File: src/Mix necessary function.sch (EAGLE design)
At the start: 15 parts, among them CON1 XT90PW-M, SW1 02-JST, SW2 02-JST

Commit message: servo2
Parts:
- added LED_SW: SS-12SDP2, SS-12SDP2:SS-12SDP2
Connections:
- new net BLUE: LED.1, LED_SW.L
- new net RED: LED.2, LED_SW.R
- net GND: now also LED_SW.C; no longer LED.1, LED.3
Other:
- note added: "servo(DS3235sg)： voltage 4.8-6.4V current about0.3A regulater 22.2Vから6Vに変圧 allowable loss(許容損失) 16W (22.2-6)*0.3=4.86W no problem"
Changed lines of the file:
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@@
 <part name="C3" library="GRM0335C1E240GA01D" deviceset="GRM0335C1E240GA01D" device="" value="0.1μF"/>
 <part name="C6" library="GRM0335C1E240GA01D" deviceset="GRM0335C1E240GA01D" device="" value="0.1μF"/>
+<part name="LED_SW" library="SS-12SDP2" deviceset="SS-12SDP2" device=""/>
 </parts>
 <sheets>
@@
 <text x="116.84" y="127" size="5.08" layer="97">LEDsupply</text>
 <wire x1="172.72" y1="223.52" x2="172.72" y2="154.94" width="0.1524" layer="97"/>
-<wire x1="172.72" y1="154.94" x2="241.3" y2="154.94" width="0.1524" layer="97"/>
-<wire x1="241.3" y1="154.94" x2="241.3" y2="223.52" width="0.1524" layer="97"/>
-<wire x1="241.3" y1="223.52" x2="172.72" y2="223.52" width="0.1524" layer="97"/>
+<wire x1="172.72" y1="154.94" x2="276.86" y2="154.94" width="0.1524" layer="97"/>
+<wire x1="276.86" y1="154.94" x2="276.86" y2="223.52" width="0.1524" layer="97"/>
+<wire x1="276.86" y1="223.52" x2="172.72" y2="223.52" width="0.1524" layer="97"/>
 <text x="175.26" y="218.44" size="5.08" layer="97">series_regulater</text>
-<text x="180.34" y="157.48" size="1.9304" layer="94">PVCC:22.2V</text>
+<text x="254" y="167.64" size="1.9304" layer="94">PVCC:22.2V</text>
 <wire x1="213.36" y1="88.9" x2="213.36" y2="137.16" width="0.1524" layer="97"/>
 <wire x1="213.36" y1="137.16" x2="266.7" y2="137.16" width="0.1524" layer="97"/>
@@
 ・テープLED用の四心コネクタ
 ・非常停止スイッチ用のAnｄ回路</text>
+<text x="241.3" y="190.5" size="1.778" layer="94">servo(DS3235sg)：
+  voltage 4.8-6.4V
+　current about0.3A
+regulater
+ 22.2Vから6Vに変圧
+ allowable loss(許容損失) 16W
+(22.2-6)*0.3=4.86W
+no problem</text>
 </plain>
 <instances>
@@
 <instance part="P+3" gate="VCC" x="177.8" y="121.92" smashed="yes"/>
 <instance part="P+4" gate="VCC" x="200.66" y="121.92" smashed="yes"/>
-<instance part="SUPPLY4" gate="GND" x="142.24" y="99.06" smashed="yes"/>
+<instance part="SUPPLY4" gate="GND" x="152.4" y="99.06" smashed="yes"/>
 <instance part="U$17" gate="G$1" x="208.28" y="180.34" smashed="yes"/>
 <instance part="C4" gate="G$1" x="193.04" y="175.26" smashed="yes">
@@
 <attribute name="NAME" x="230.124" y="175.641" size="1.778" layer="95"/>
 <attribute name="VALUE" x="230.124" y="170.561" size="1.778" layer="96"/>
+</instance>
+<instance part="LED_SW" gate="G$1" x="147.32" y="104.14" smashed="yes" rot="R90">
+<attribute name="NAME" x="152.4" y="101.6" size="1.778" layer="95" rot="R180"/>
 </instance>
 </instances>
@@
 </segment>
 <segment>
-<pinref part="LED" gate="G$1" pin="3"/>
-<wire x1="134.62" y1="109.22" x2="142.24" y2="109.22" width="0.1524" layer="91"/>
-<pinref part="SUPPLY4" gate="GND" pin="GND"/>
-<pinref part="LED" gate="G$1" pin="1"/>
-<wire x1="142.24" y1="109.22" x2="142.24" y2="104.14" width="0.1524" layer="91"/>
-<wire x1="142.24" y1="104.14" x2="142.24" y2="101.6" width="0.1524" layer="91"/>
-<wire x1="134.62" y1="104.14" x2="142.24" y2="104.14" width="0.1524" layer="91"/>
-<junction x="142.24" y="104.14"/>
-<label x="139.7" y="96.52" size="1.778" layer="95"/>
-</segment>
-<segment>
 <pinref part="AZUSA_CON" gate="G$1" pin="1"/>
 <wire x1="236.22" y1="119.38" x2="241.3" y2="119.38" width="0.1524" layer="91"/>
@@
 <label x="205.74" y="187.96" size="1.778" layer="95"/>
 </segment>
+<segment>
+<pinref part="LED_SW" gate="G$1" pin="C"/>
+<pinref part="SUPPLY4" gate="GND" pin="GND"/>
+<wire x1="152.4" y1="104.14" x2="152.4" y2="101.6" width="0.1524" layer="91"/>
+<label x="149.86" y="96.52" size="1.778" layer="95"/>
+</segment>
 </net>
 <net name="VCC" class="0">
@@
 </segment>
 </net>
+<net name="RED" class="0">
+<segment>
+<pinref part="LED" gate="G$1" pin="2"/>
+<wire x1="134.62" y1="106.68" x2="142.24" y2="106.68" width="0.1524" layer="91"/>
+<pinref part="LED_SW" gate="G$1" pin="R"/>
+<label x="137.16" y="106.68" size="1.778" layer="95"/>
+</segment>
+</net>
+<net name="BLUE" class="0">
+<segment>
+<pinref part="LED" gate="G$1" pin="1"/>
+<wire x1="134.62" y1="104.14" x2="134.62" y2="101.6" width="0.1524" layer="91"/>
+<pinref part="LED_SW" gate="G$1" pin="L"/>
+<wire x1="134.62" y1="101.6" x2="142.24" y2="101.6" width="0.1524" layer="91"/>
+<label x="137.16" y="101.6" size="1.778" layer="95"/>
+</segment>
+</net>

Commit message: necefunc fix
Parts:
- added AZUSA_CON2: 02-JST, con-jst-xh (1):02-JST
- added H1, H2, H3, H4: MOUNT-HOLE3.2, holes:MOUNT-HOLE3.2
- added SERVO2: (no value), con-jst-xh (1):03-JST
- renumbered AZUSA_CON to AZUSA_CON1, SERVO to SERVO1
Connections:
- net PWM_SERVO renamed PWM1_SERVO
- new net PWM2_SERVO: AZUSA_CON2.2, SERVO2.3
- net +6V: now also SERVO2.2
- net GND: now also AZUSA_CON2.1, SERVO2.1
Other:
- note added: "drill"

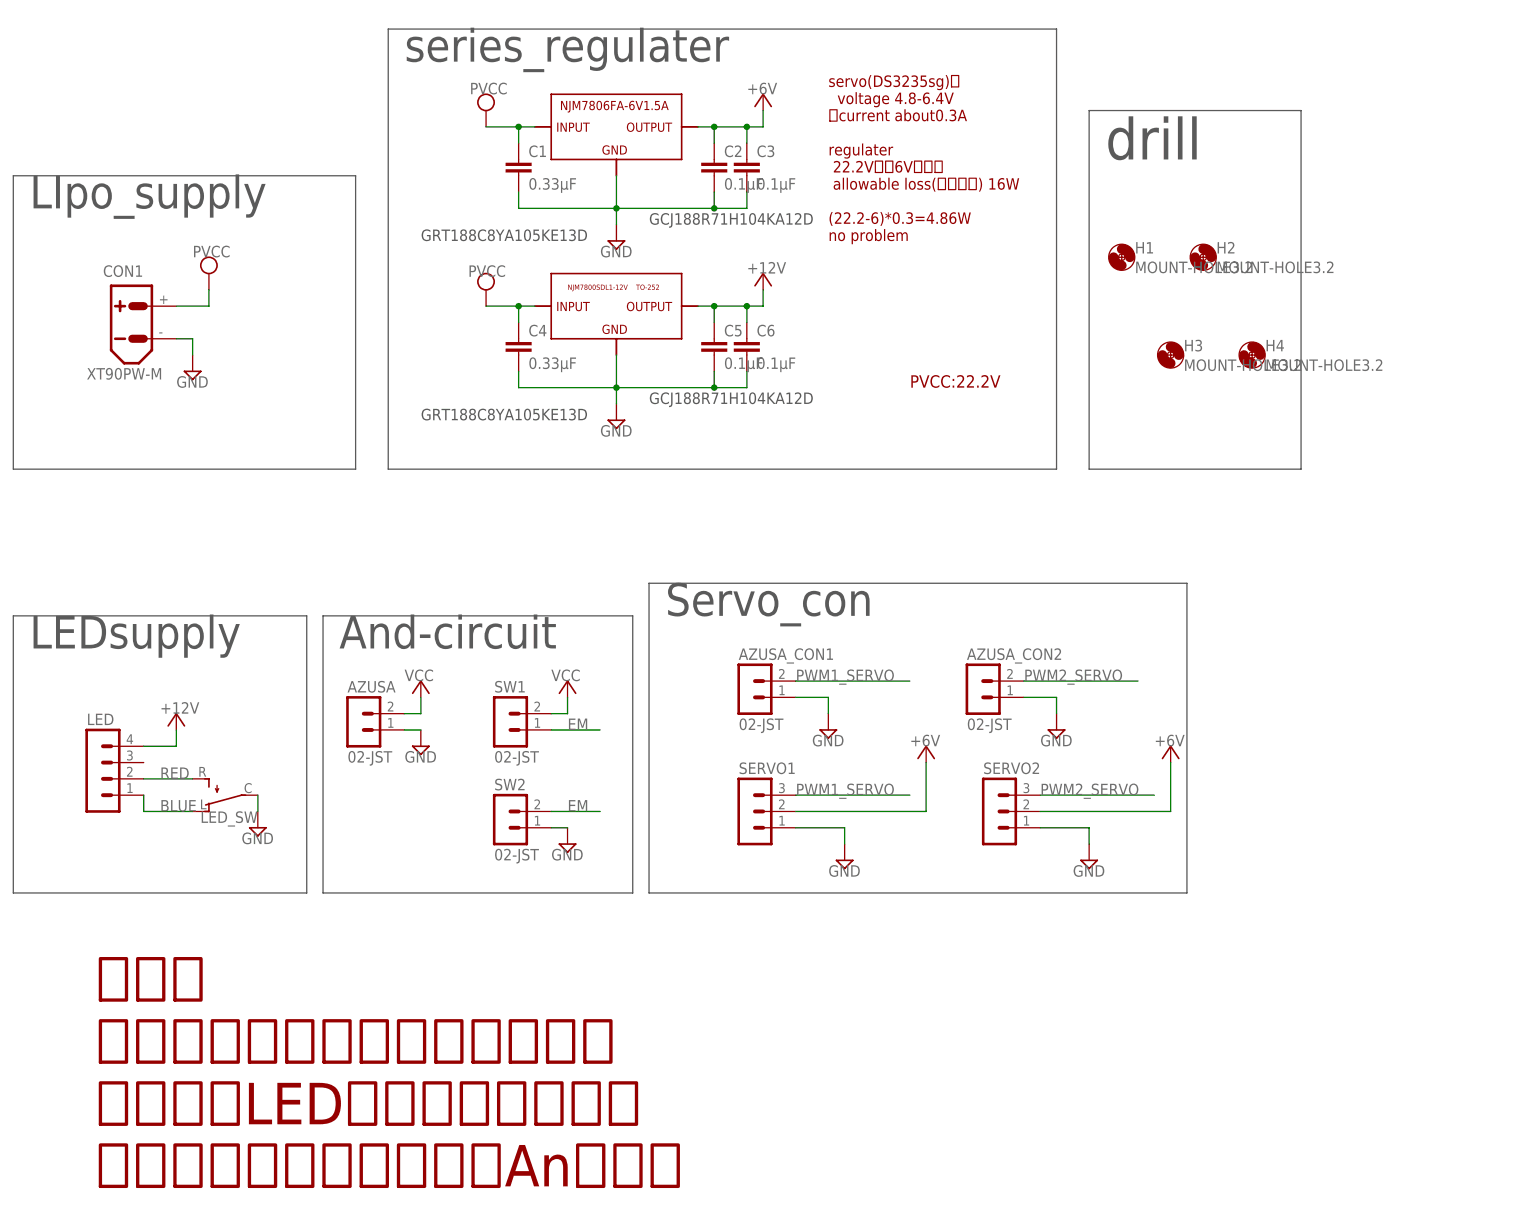
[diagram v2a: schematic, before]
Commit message: fix twelite circuit slot
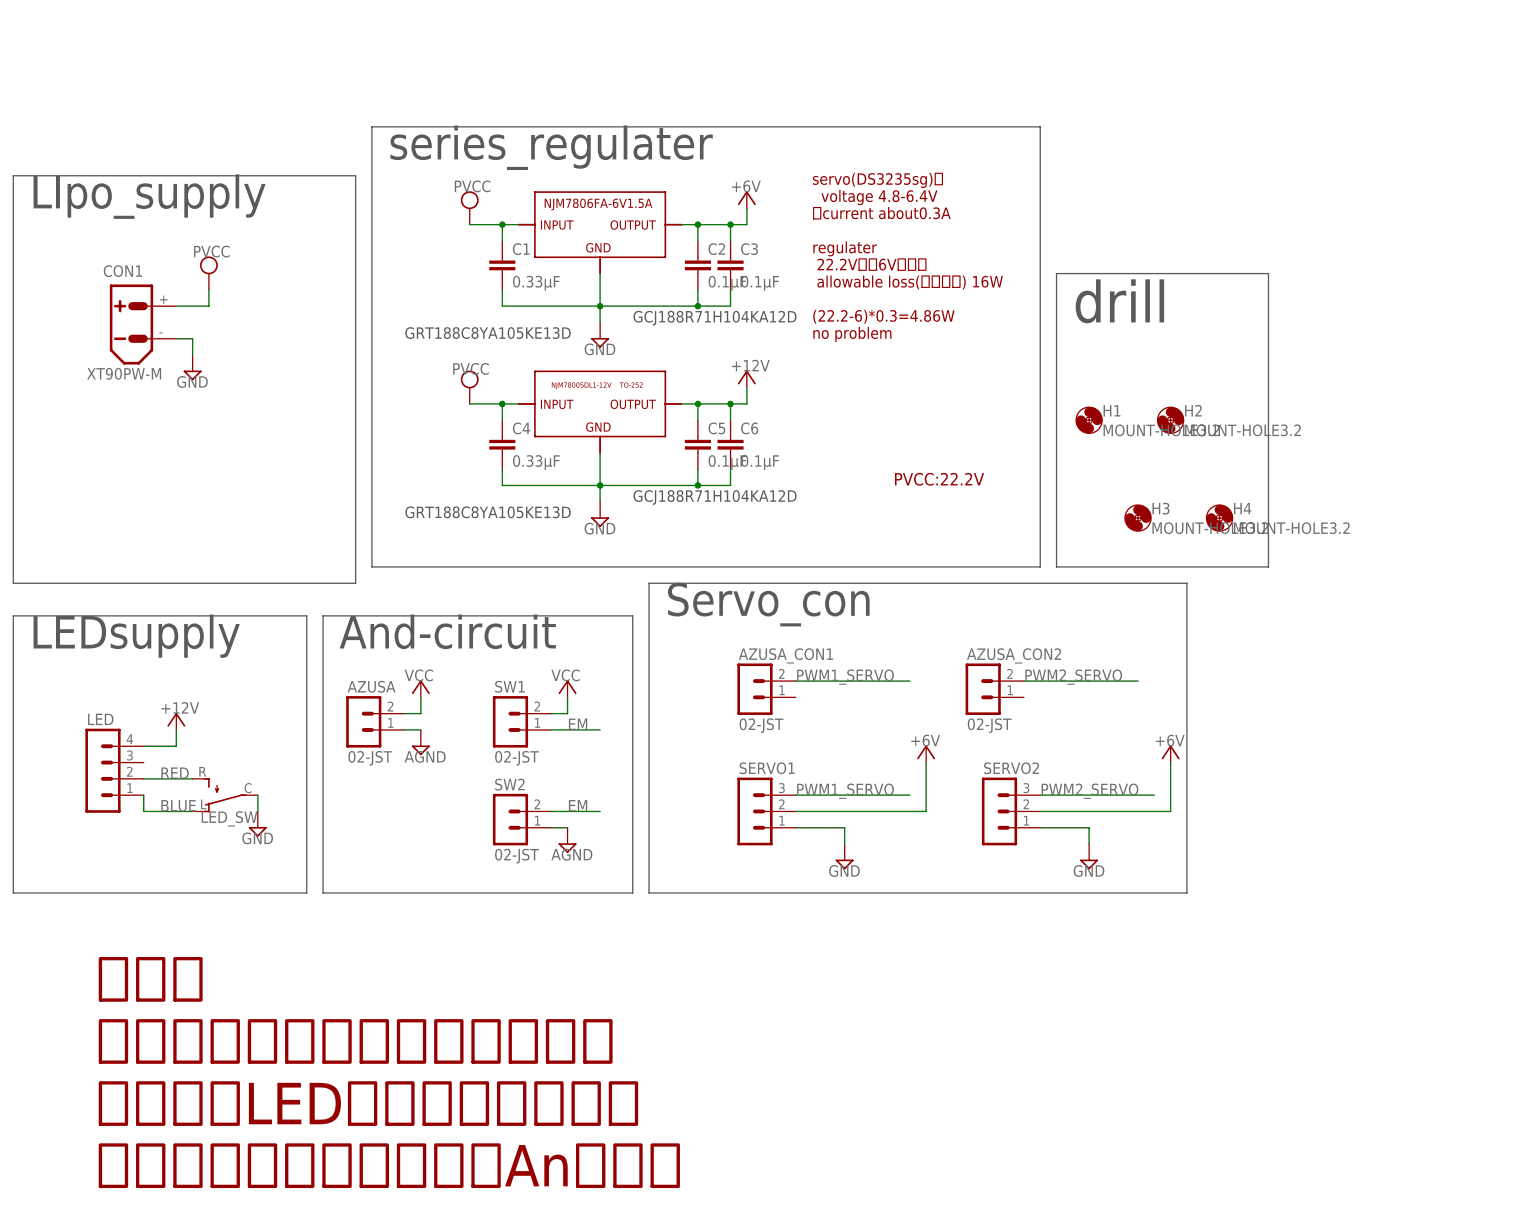
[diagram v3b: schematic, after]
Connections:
- new net AGND: AZUSA.1, SW2.1
- net GND: no longer AZUSA.1, AZUSA_CON1.1, AZUSA_CON2.1, SW2.1
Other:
- moved on the sheet: C1, C2, C3, C4, C5, C6, H1, H2, H3, H4

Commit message: add servo emergency
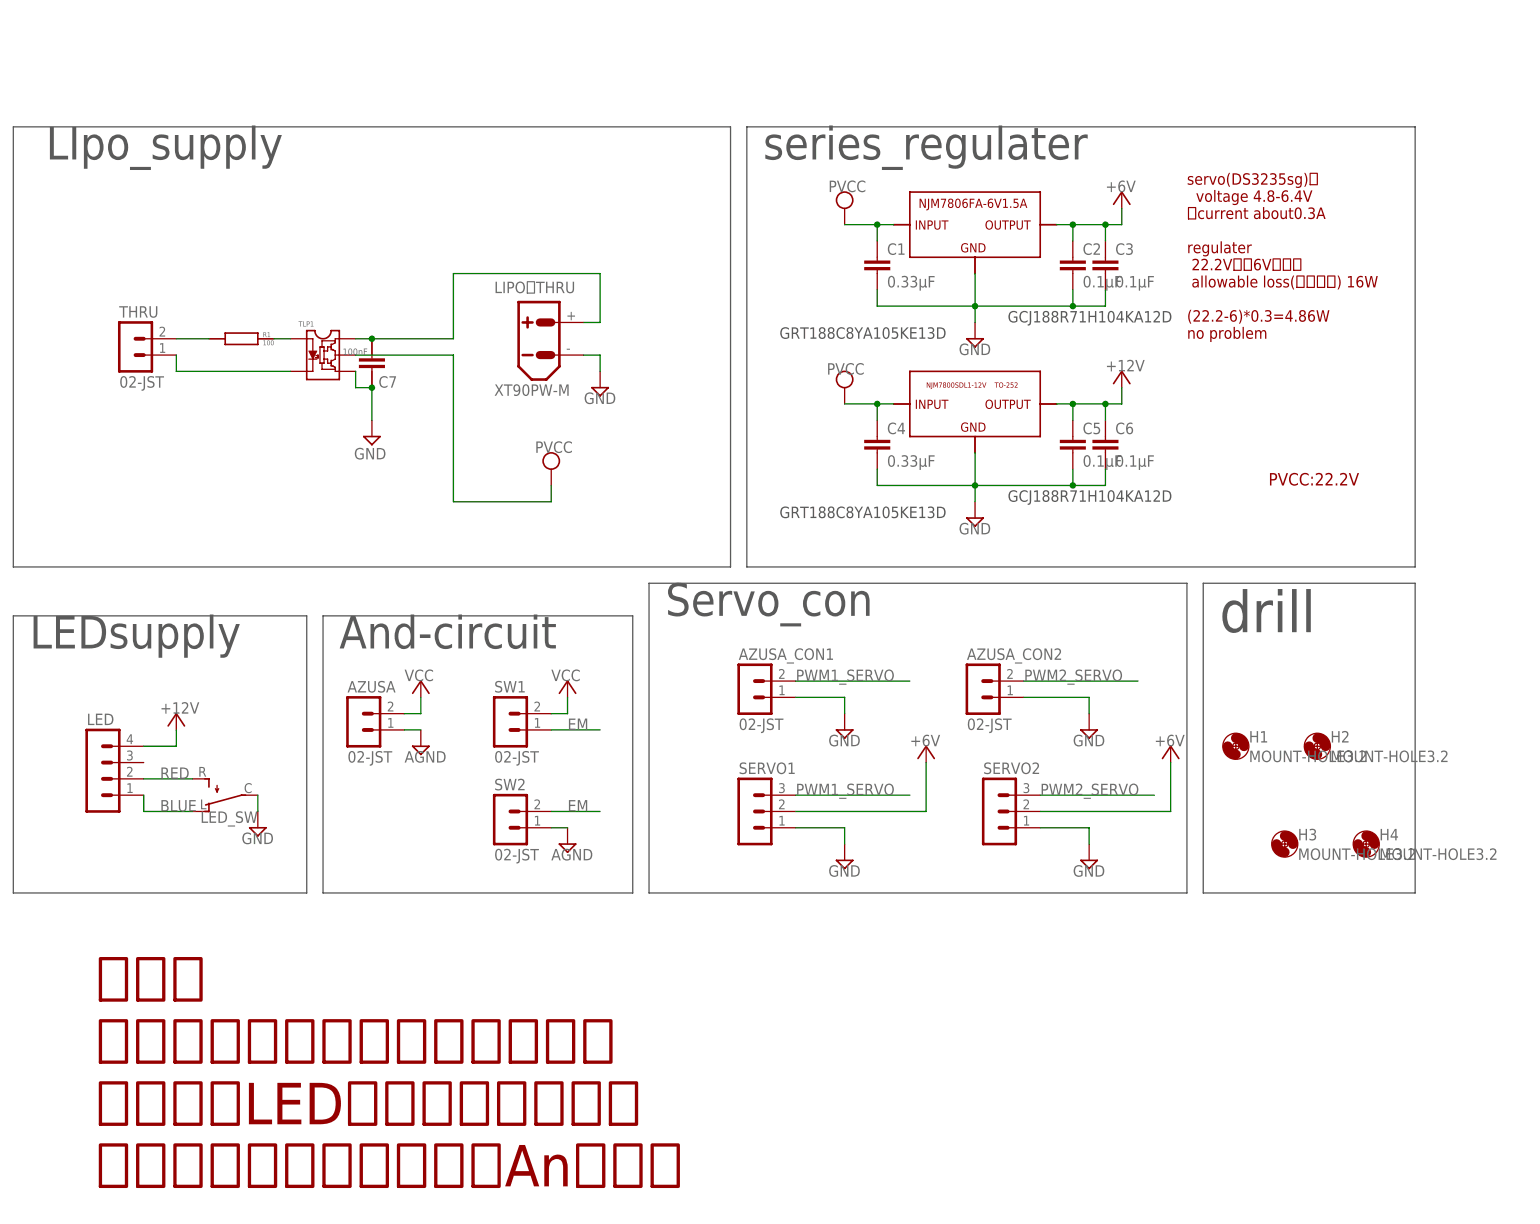
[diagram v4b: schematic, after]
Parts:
- removed CON1: XT90PW-M, amass:XT90PW-M
- added C7: GCM188L81H104KA57, GCM188L81H104K57(0.1uF):GCM188L81H104KA57
- added LIPO＿THRU: XT90PW-M, amass:XT90PW-M
- added R1: 100, CR0603:CR0603
- added THRU: 02-JST, con-jst-xh (1):02-JST
- added TLP1: TLP152, TLP152:TLP152
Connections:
- new net N$1: THRU.1, TLP1.CATHODE
- new net N$118: R1.RIGHT, TLP1.ANODE
- new net N$20: C7.P$1, LIPO＿THRU.+, TLP1.VCC
- new net N$92: R1.LEFT, THRU.2
- net GND: now also AZUSA_CON1.1, AZUSA_CON2.1, C7.P$2, LIPO＿THRU.-, TLP1.GND; no longer CON1.-
- net PVCC: now also TLP1.VOUT; no longer CON1.+
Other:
- note added: "機能： ・サーボモータ用三芯コネクタ ・テープLED用の四芯コネクタ ・非常停止スイッチ用のAnｄ回路"
- note removed: "機能： ・サーボモータ用三心コネクタ ・テープLED用の四心コネクタ ・非常停止スイッチ用のAnｄ回路"
- moved on the sheet: C1, C2, C3, C4, C5, C6, H1, H2, H3, H4

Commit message: fix
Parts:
- added D1: GS2M-LTP, GS2M-LTP:GS2M-LTP
- added Q1: SQJA16EP-T1_GE3, SQJA16EP-T1_GE3:SQJA16EP-T1_GE3
- added R2: 820, CR0603:CR0603
- added R3: 10, CR0603:CR0603
- added R4: 10k, CR0603:CR0603
- added ZD1: MMBZ5248B-TP, MMBZ5248B-TP:MMBZ5248B-TP
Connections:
- new net N$6: D1.C, R2.LEFT, TLP1.VOUT
- new net N$7: Q1.G, R2.RIGHT, R3.RIGHT, R4.RIGHT, ZD1.C
- new net N$8: D1.A, R3.LEFT
- net N$20: now also Q1.D
- net PVCC: now also Q1.S, R4.LEFT, ZD1.A; no longer TLP1.VOUT
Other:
- note added: "servoの非常停止機能の接続用コネクタ"
- note added: "逆方向漏れ防止"
- moved on the sheet: C7, LIPO＿THRU, R1, THRU, TLP1
